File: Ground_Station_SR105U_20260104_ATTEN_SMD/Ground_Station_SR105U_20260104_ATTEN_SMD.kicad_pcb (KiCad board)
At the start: 2 copper layers, 90.2 x 95.9 mm, 136 parts, among them J10 SC1464-ND, J11 SC1464-ND, J12 SQ, J2 SQ, J3 Conn_02x03_Odd_Even, J4 Conn_01x03, J5 Conn_01x03, J6 Conn_02x03_Odd_Even, J7 SQ, J8 Conn_01x20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

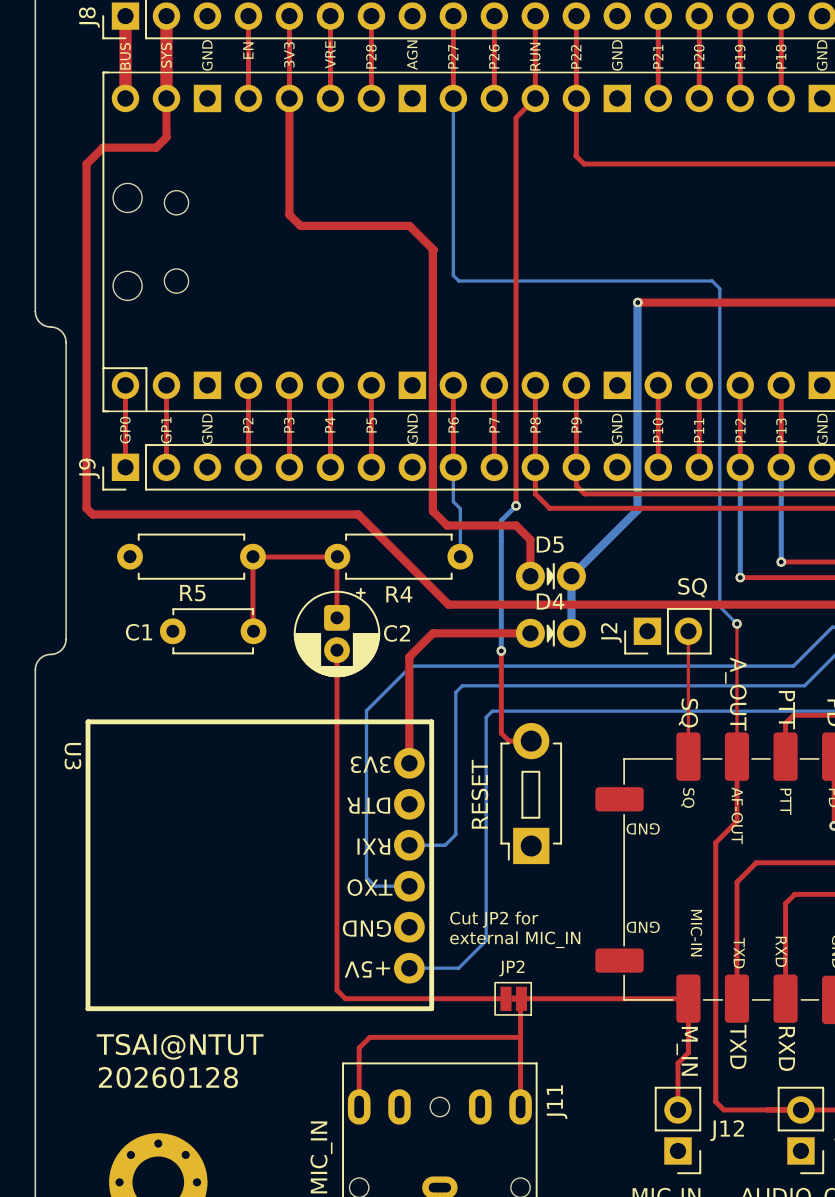
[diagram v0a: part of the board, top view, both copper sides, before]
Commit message: Add test points for audio filter
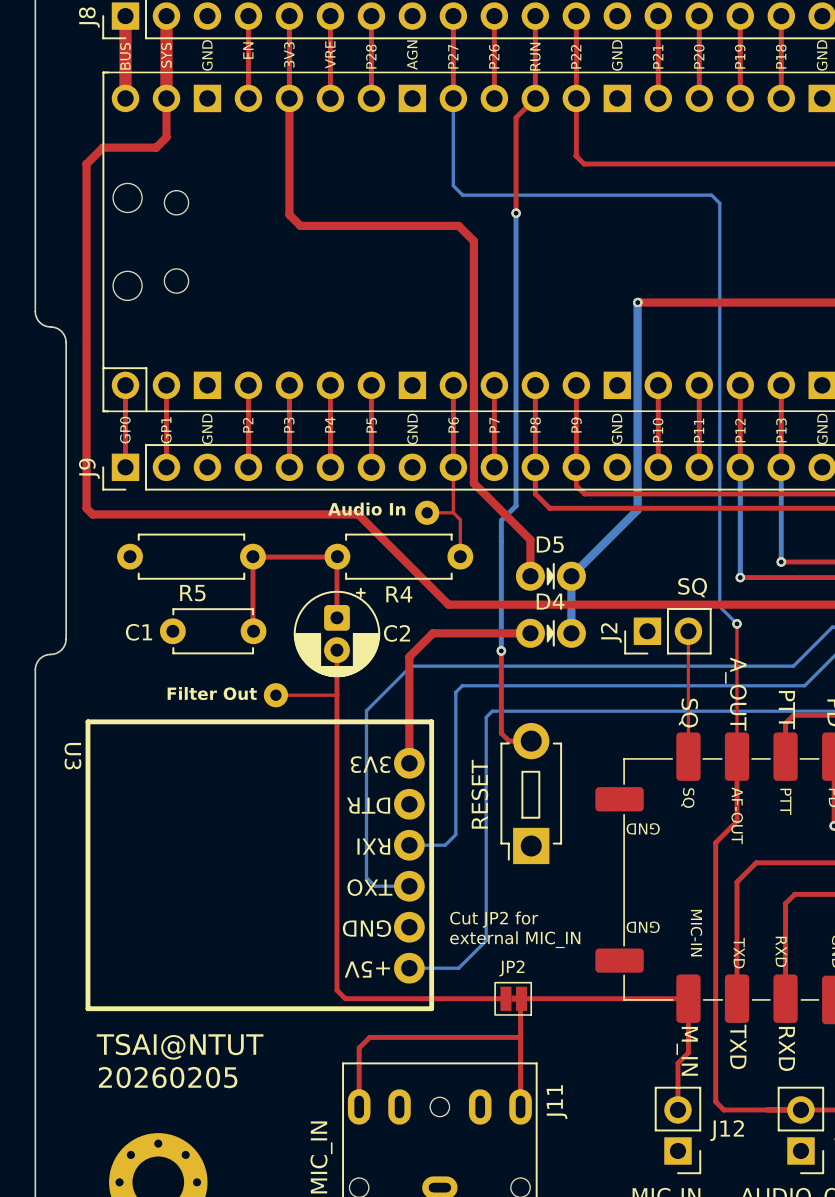
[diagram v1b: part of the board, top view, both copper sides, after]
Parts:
- added TP1: Audio_Out, AMSAT:TestPoint_THTPad_D1.5mm_Drill0.7mm, F.Cu at (86.5, 105.7)
- added TP2: Filter_Out, AMSAT:TestPoint_THTPad_D1.5mm_Drill0.7mm, F.Cu at (77.1, 117.0)
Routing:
- net /FILTER_OUT: track 31.8 -> 35.6 mm
- net /AUDIO_OUT: track 10.8 -> 12.4 mm
- net /3V3_PICO: track 47.4 -> 46.6 mm
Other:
- board text added: "Audio In"
- board text added: "Filter Out"
- board text added: "TSAI@NTUT 20260205"
- board text removed: "TSAI@NTUT 20260128"
